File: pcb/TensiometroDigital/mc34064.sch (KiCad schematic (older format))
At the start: 1 part

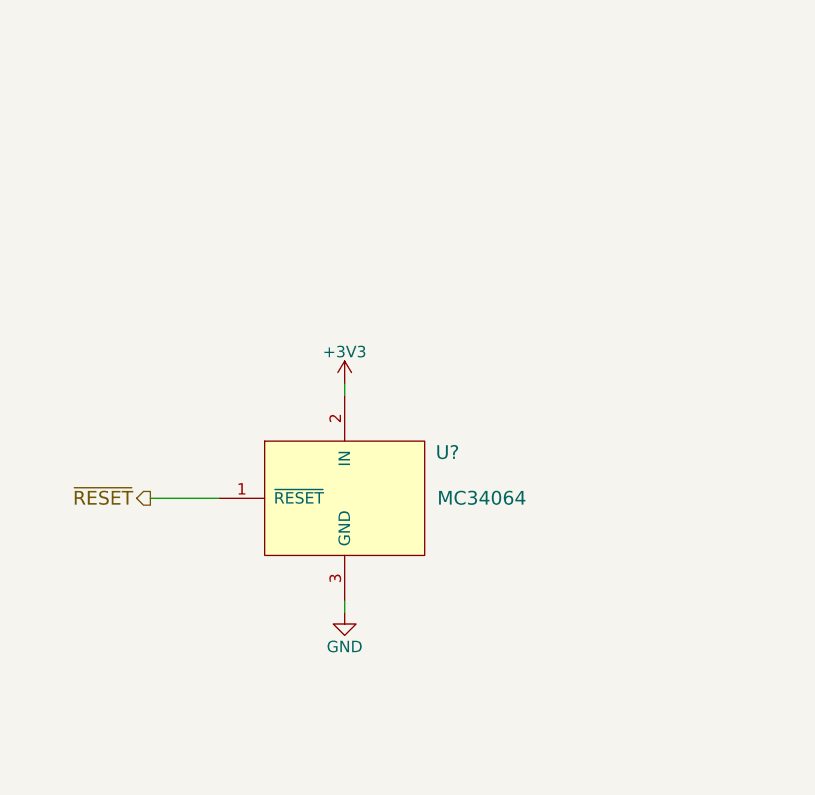
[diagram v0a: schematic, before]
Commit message: Finalizado: SCH, PCB, GABINETE, DRAWINGS. FALTA: GERBERS, BOM e Informe
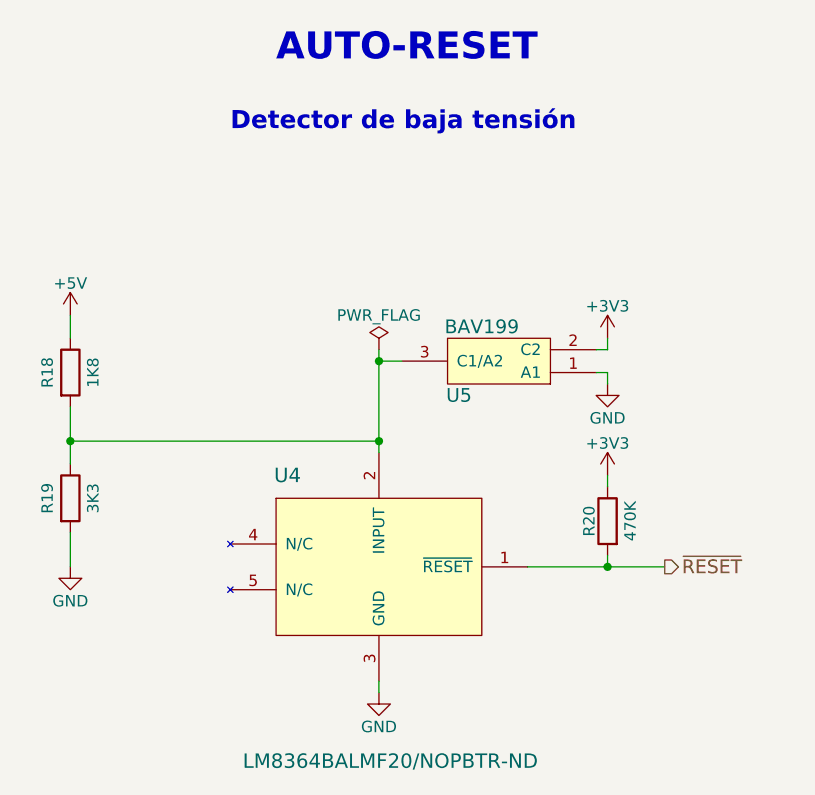
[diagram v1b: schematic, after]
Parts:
- removed U?: MC34064, symbol MC34064
- added R18: 1K8, Resistors_SMD:R_0805_HandSoldering, symbol R
- added R19: 3K3, Resistors_SMD:R_0805_HandSoldering, symbol R
- added R20: 470K, Resistors_SMD:R_0805_HandSoldering, symbol R
- added U4: LM8364BALMF20/NOPBTR-ND, TO_SOT_Packages_SMD:SOT-23-5_HandSoldering, symbol LM8364
- added U5: BAV199, TO_SOT_Packages_SMD:SOT-23, symbol BAV199
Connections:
- net +3V3: now also R20.1, U5.2 (C2)
- net GND: now also R19.2, U4.3 (GND), U5.1 (A1)
- net ~RESET: now also R20.2, U4.1 (~RESET)
- new net: R18.2, R19.1, U4.2 (INPUT), U5.3 (C1/A2)
- new net +5V: R18.1
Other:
- note added: "AUTO-RESET"
- note added: "Detector de baja tensión"
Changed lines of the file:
@@
 LIBS:lm2940
 LIBS:lm2575
+LIBS:bav199
+LIBS:mpxv5050gp
+LIBS:lm8364
 LIBS:TensiometroDigital-cache
 EELAYER 25 0
@@
 $Descr A4 11693 8268
 encoding utf-8
-Sheet 5 8
-Title ""
-Date ""
-Rev ""
-Comp ""
-Comment1 ""
-Comment2 ""
-Comment3 ""
-Comment4 ""
+Sheet 4 11
+Title "TENSIÓMETRO DIGITAL"
+Date "2018-11-20"
+Rev "A"
+Comp "UTN - FRBA"
+Comment1 "Curso: R1032"
+Comment2 "Leg.: 153204-2"
+Comment3 "Autor: Alegre Mendoza Ezequiel"
+Comment4 "SDR Proyecto Final"
 $EndDescr
-Wire Wire Line
-	5650 3250 5650 3300
 $Comp
-L GND #PWR?
+L GND #PWR08
 U 1 1 5BBE3D6B
-P 5650 4250
-F 0 "#PWR?" H 5650 4000 50  0001 C CNN
-F 1 "GND" H 5650 4100 50  0000 C CNN
-F 2 "" H 5650 4250 50  0001 C CNN
-F 3 "" H 5650 4250 50  0001 C CNN
-	1    5650 4250
+P 5800 4600
+F 0 "#PWR08" H 5800 4350 50  0001 C CNN
+F 1 "GND" H 5800 4450 50  0000 C CNN
+F 2 "" H 5800 4600 50  0001 C CNN
+F 3 "" H 5800 4600 50  0001 C CNN
+	1    5800 4600
+	1    0    0    -1
+$EndComp
+Text HLabel 7050 4050 2    60   Output ~ 0
+~RESET
+Text Notes 5350 1850 0    118  ~ 24
+AUTO-RESET
+Text Notes 5150 2150 0    79   ~ 16
+Detector de baja tensión
+$Comp
+L LM8364 U4
+U 1 1 5BDC9851
+P 5350 3800
+F 0 "U4" H 5400 3950 63  0000 C CNN
+F 1 "LM8364BALMF20/NOPBTR-ND" H 5850 2700 63  0000 C CNN
+F 2 "TO_SOT_Packages_SMD:SOT-23-5_HandSoldering" H 5350 3800 118 0001 C CNN
+F 3 "" H 5350 3800 118 0001 C CNN
+F 4 "LM8364BALMF20/NOPB " H 5350 3800 60  0001 C CNN "manf#"
+	1    5350 3800
+	1    0    0    -1
+$EndComp
+$Comp
+L R R18
+U 1 1 5BDBCD07
+P 4450 3200
+F 0 "R18" V 4350 3200 50  0000 C CNN
+F 1 "1K8" V 4550 3200 50  0000 C CNN
+F 2 "Resistors_SMD:R_0805_HandSoldering" V 4380 3200 50  0001 C CNN
+F 3 "" H 4450 3200 50  0001 C CNN
+F 4 "RT0805DRD071K8L" V 4450 3200 60  0001 C CNN "manf#"
+	1    4450 3200
+	1    0    0    -1
+$EndComp
+$Comp
+L R R19
+U 1 1 5BDBCD52
+P 4450 3750
+F 0 "R19" V 4350 3750 50  0000 C CNN
+F 1 "3K3" V 4550 3750 50  0000 C CNN
+F 2 "Resistors_SMD:R_0805_HandSoldering" V 4380 3750 50  0001 C CNN
+F 3 "" H 4450 3750 50  0001 C CNN
+F 4 "SG73G2ATTD3301D" V 4450 3750 60  0001 C CNN "manf#"
+	1    4450 3750
+	1    0    0    -1
+$EndComp
+$Comp
+L +5V #PWR09
+U 1 1 5BDBCDA9
+P 4450 2950
+F 0 "#PWR09" H 4450 2800 50  0001 C CNN
+F 1 "+5V" H 4450 3090 50  0000 C CNN
+F 2 "" H 4450 2950 50  0001 C CNN
+F 3 "" H 4450 2950 50  0001 C CNN
+	1    4450 2950
+	1    0    0    -1
+$EndComp
+$Comp
+L GND #PWR010
+U 1 1 5BDBCDCB
+P 4450 4050
+F 0 "#PWR010" H 4450 3800 50  0001 C CNN
+F 1 "GND" H 4450 3900 50  0000 C CNN
+F 2 "" H 4450 4050 50  0001 C CNN
+F 3 "" H 4450 4050 50  0001 C CNN
+	1    4450 4050
+	1    0    0    -1
+$EndComp
+$Comp
+L BAV199 U5
+U 1 1 5BDBD55A
+P 6550 3250
+F 0 "U5" H 6950 3300 60  0000 C CNN
+F 1 "BAV199" H 6850 3000 60  0000 C CNN
+F 2 "TO_SOT_Packages_SMD:SOT-23" H 6550 3250 60  0001 C CNN
+F 3 "" H 6550 3250 60  0001 C CNN
+F 4 "BAV199HMFHT116" H 6550 3250 60  0001 C CNN "manf#"
+	1    6550 3250
+	-1   0    0    1
+$EndComp
+$Comp
+L +3V3 #PWR011
+U 1 1 5BDBD5D2
+P 6800 3050
+F 0 "#PWR011" H 6800 2900 50  0001 C CNN
+F 1 "+3V3" H 6800 3190 50  0000 C CNN
+F 2 "" H 6800 3050 50  0001 C CNN
+F 3 "" H 6800 3050 50  0001 C CNN
+	1    6800 3050
+	1    0    0    -1
+$EndComp
+$Comp
+L GND #PWR012
+U 1 1 5BDBD5EE
+P 6800 3250
+F 0 "#PWR012" H 6800 3000 50  0001 C CNN
+F 1 "GND" H 6800 3100 50  0000 C CNN
+F 2 "" H 6800 3250 50  0001 C CNN
+F 3 "" H 6800 3250 50  0001 C CNN
+	1    6800 3250
+	1    0    0    -1
+$EndComp
+$Comp
+L R R20
+U 1 1 5BDC9F61
+P 6800 3850
+F 0 "R20" V 6880 3850 50  0000 C CNN
+F 1 "470K" V 6700 3850 50  0000 C CNN
+F 2 "Resistors_SMD:R_0805_HandSoldering" V 6730 3850 50  0001 C CNN
+F 3 "" H 6800 3850 50  0001 C CNN
+F 4 "RT0805DRD07470KL" V 6800 3850 60  0001 C CNN "manf#"
+	1    6800 3850
+	-1   0    0    -1
+$EndComp
+$Comp
+L +3V3 #PWR013
+U 1 1 5BDC9FED
+P 6800 3650
+F 0 "#PWR013" H 6800 3500 50  0001 C CNN
+F 1 "+3V3" H 6800 3790 50  0000 C CNN
+F 2 "" H 6800 3650 50  0001 C CNN
+F 3 "" H 6800 3650 50  0001 C CNN
+	1    6800 3650
 	1    0    0    -1
 $EndComp
 Wire Wire Line
-	5650 4250 5650 4200
+	5800 4600 5800 4550
 Wire Wire Line
-	5100 3750 4800 3750
-Text HLabel 4800 3750 0    60   Output ~ 0
-~RESET
+	6450 4050 7050 4050
+Wire Wire Line
+	4450 3350 4450 3600
+Wire Wire Line
+	4450 2950 4450 3050
+Wire Wire Line
+	4450 4050 4450 3900
+Wire Wire Line
+	4450 3500 5800 3500
+Connection ~ 4450 3500
+Wire Wire Line
+	5800 3100 5800 3550
+Wire Wire Line
+	5900 3150 5800 3150
+Connection ~ 5800 3500
+Wire Wire Line
+	6800 3250 6800 3200
+Wire Wire Line
+	6800 3200 6750 3200
+Wire Wire Line
+	6750 3100 6800 3100
+Wire Wire Line
+	6800 3100 6800 3050
+Wire Wire Line
+	6800 4000 6800 4050
+Connection ~ 6800 4050
+Wire Wire Line
+	6800 3650 6800 3700
 $Comp
-L MC34064 U?
-U 1 1 5BBE3C81
-P 5300 3500
-F 0 "U?" H 6100 3450 60  0000 C CNN
-F 1 "MC34064" H 6250 3250 60  0000 C CNN
-F 2 "" H 5300 3500 60  0001 C CNN
-F 3 "" H 5300 3500 60  0001 C CNN
-	1    5300 3500
+L PWR_FLAG #FLG014
+U 1 1 5BDD0713
+P 5800 3100
+F 0 "#FLG014" H 5800 3175 50  0001 C CNN
+F 1 "PWR_FLAG" H 5800 3250 50  0000 C CNN
+F 2 "" H 5800 3100 50  0001 C CNN
+F 3 "" H 5800 3100 50  0001 C CNN
+	1    5800 3100
 	1    0    0    -1
 $EndComp
-$Comp
-L +3V3 #PWR?
-U 1 1 5BBF84ED
-P 5650 3250
-F 0 "#PWR?" H 5650 3100 50  0001 C CNN
-F 1 "+3V3" H 5650 3390 50  0000 C CNN
-F 2 "" H 5650 3250 50  0001 C CNN
-F 3 "" H 5650 3250 50  0001 C CNN
-	1    5650 3250
-	1    0    0    -1
-$EndComp
+Connection ~ 5800 3150
 $EndSCHEMATC

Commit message: Creada la BOM
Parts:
- R20: manf# RT0805DRD07470KL -> KTR10EZPF4703
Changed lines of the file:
@@
 F 2 "Resistors_SMD:R_0805_HandSoldering" V 6730 3850 50  0001 C CNN
 F 3 "" H 6800 3850 50  0001 C CNN
-F 4 "RT0805DRD07470KL" V 6800 3850 60  0001 C CNN "manf#"
+F 4 "KTR10EZPF4703" V 6800 3850 60  0001 C CNN "manf#"
 	1    6800 3850
 	-1   0    0    -1
